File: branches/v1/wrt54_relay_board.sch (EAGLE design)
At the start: 61 parts, among them IC1 18F2550, IC2 786TV, IC3 MAX232, K1 351, K2 351, T1 2STX1360, T2 2STX1360, X1 C-GRID-05-70543

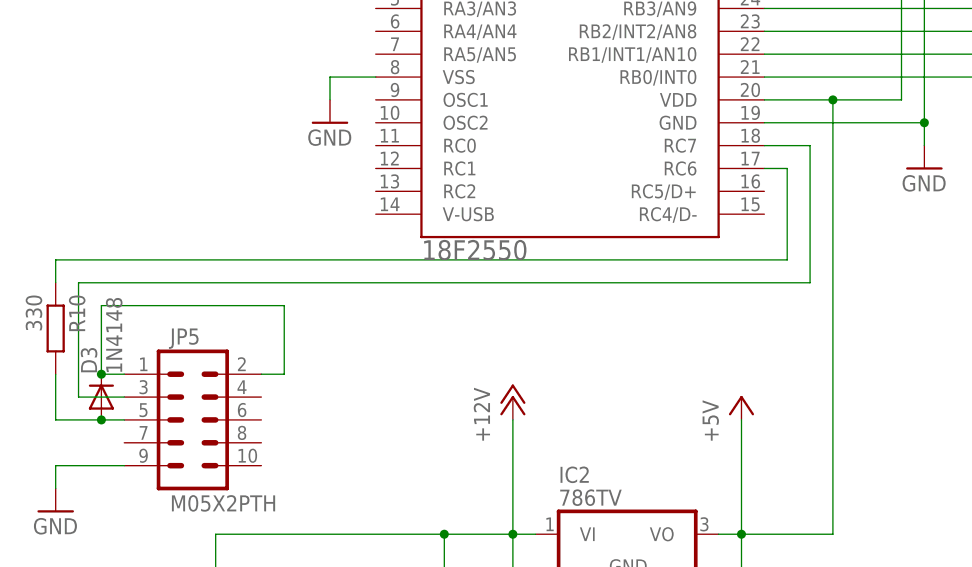
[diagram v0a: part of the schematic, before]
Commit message: added missing resistor between wrt54-tx and pic-rx - it burned the tx port twice :-(
added flush command to delete all rfid
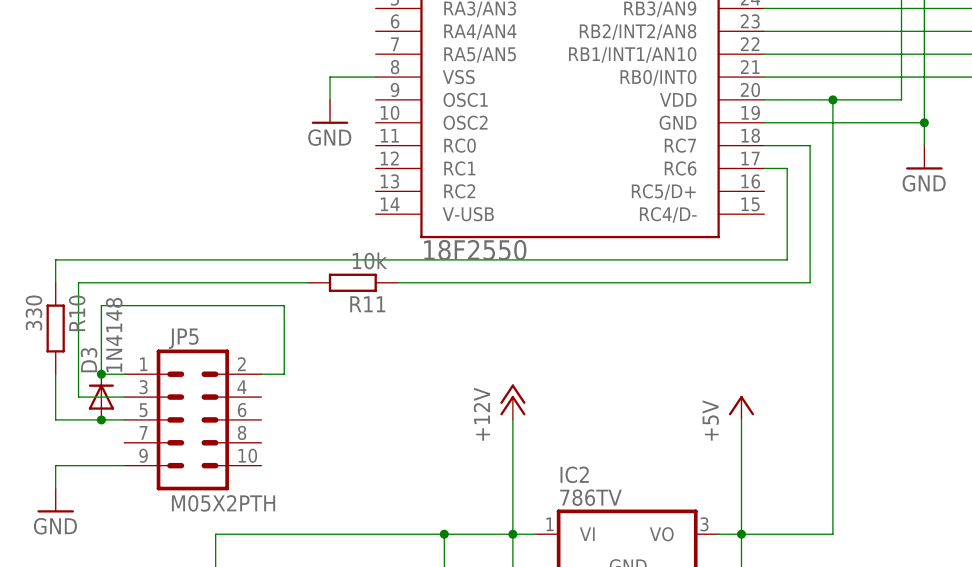
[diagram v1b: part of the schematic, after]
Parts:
- added R11: 10k, resistor:R-EU_0204/2V
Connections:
- new net N$39: JP5.3, R11.2
- net N$25: now also R11.1; no longer JP5.3
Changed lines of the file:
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@@
 <part name="P+9" library="supply1" deviceset="+5V" device=""/>
 <part name="GND12" library="supply1" deviceset="GND" device=""/>
+<part name="R11" library="resistor" deviceset="R-EU_" device="0204/2V" value="10k"/>
 </parts>
 <sheets>
@@
 <instance part="P+9" gate="1" x="152.4" y="-58.42"/>
 <instance part="GND12" gate="1" x="180.34" y="-68.58"/>
+<instance part="R11" gate="G$1" x="53.34" y="12.7" rot="R180"/>
 </instances>
 <busses>
@@
 <wire x1="99.06" y1="27.94" x2="104.14" y2="27.94" width="0.1524" layer="91"/>
 <wire x1="104.14" y1="27.94" x2="104.14" y2="12.7" width="0.1524" layer="91"/>
-<wire x1="104.14" y1="12.7" x2="22.86" y2="12.7" width="0.1524" layer="91"/>
-<wire x1="22.86" y1="12.7" x2="22.86" y2="0" width="0.1524" layer="91"/>
-<pinref part="JP5" gate="G$1" pin="3"/>
-<wire x1="22.86" y1="0" x2="27.94" y2="0" width="0.1524" layer="91"/>
+<pinref part="R11" gate="G$1" pin="1"/>
+<wire x1="58.42" y1="12.7" x2="104.14" y2="12.7" width="0.1524" layer="91"/>
 </segment>
 </net>
@@
 </segment>
 </net>
+<net name="N$39" class="0">
+<segment>
+<pinref part="JP5" gate="G$1" pin="3"/>
+<wire x1="22.86" y1="12.7" x2="22.86" y2="0" width="0.1524" layer="91"/>
+<wire x1="22.86" y1="0" x2="27.94" y2="0" width="0.1524" layer="91"/>
+<pinref part="R11" gate="G$1" pin="2"/>
+<wire x1="48.26" y1="12.7" x2="22.86" y2="12.7" width="0.1524" layer="91"/>
+</segment>
+</net>
